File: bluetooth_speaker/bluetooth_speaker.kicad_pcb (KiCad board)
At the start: 2 copper layers, 40 parts, among them J1 Conn_Coaxial, J2 USB_C_Receptacle_USB2.0_16P, J3 282836-4, U1 MAX98357A, U2 XL4015, U3 CP2102N-A01-GQFN28, U4 ESP32-D0WD-V3, Y1 40MHz(±10 ppm)

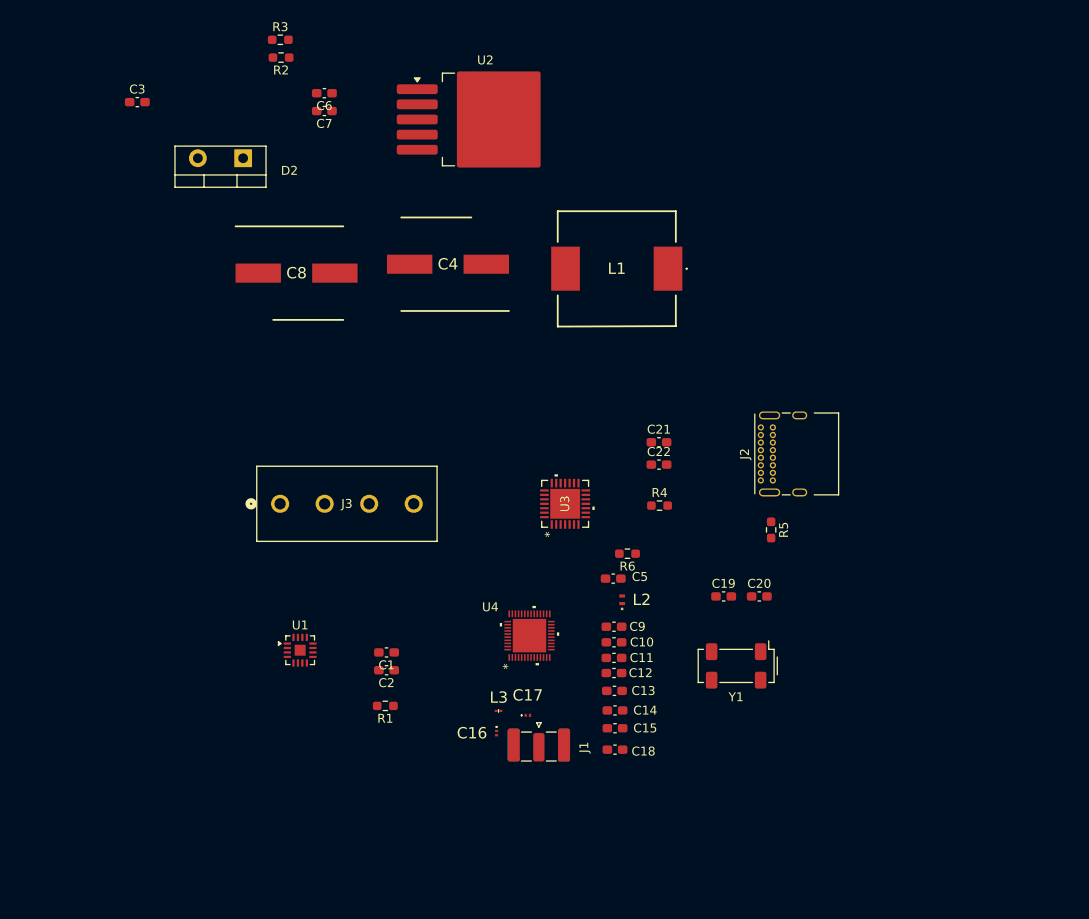
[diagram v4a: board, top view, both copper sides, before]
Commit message: Realigned components on PCB
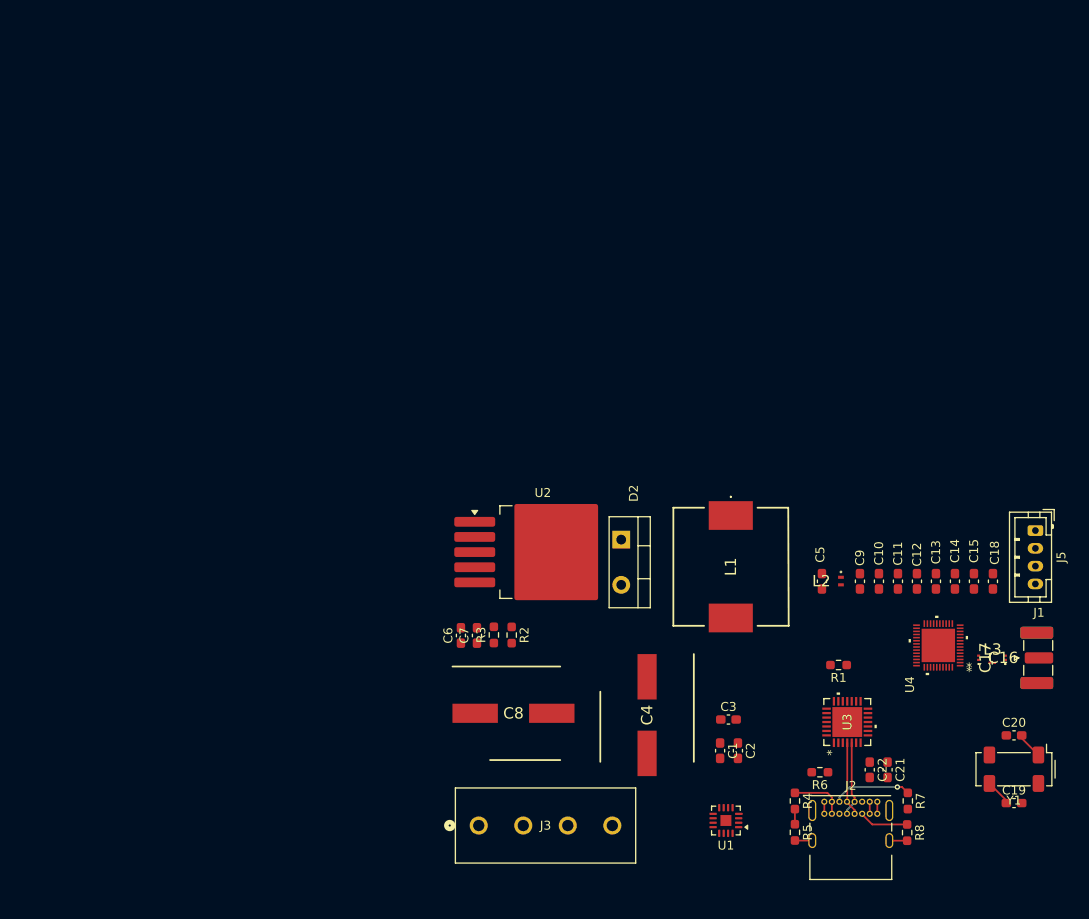
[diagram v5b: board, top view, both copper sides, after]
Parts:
- added J5: Conn_01x04_Pin, Connector_JST:JST_PH_B4B-PH-K_1x04_P2.00mm_Vertical, F.Cu at (181.0, 87.0)
- added R7: 5.1k, Resistor_SMD:R_0603_1608Metric_Pad0.98x0.95mm_HandSolder, F.Cu at (166.7, 117.4)
- added R8: 5.1k, Resistor_SMD:R_0603_1608Metric_Pad0.98x0.95mm_HandSolder, F.Cu at (166.6, 120.9)
- moved C3 96.0 mm to (146.5, 108.2)
- moved R3 71.0 mm to (120.2, 98.7), turned to 90 degrees
- moved R2 69.8 mm to (122.2, 98.7), turned to -90 degrees
- moved C6 62.8 mm to (116.5, 98.8), turned to 90 degrees
- moved C7 61.3 mm to (118.3, 98.8), turned to 90 degrees
- moved D2 60.3 mm to (134.5, 88.0), turned to -90 degrees
- moved J1 57.0 mm to (181.4, 101.3), turned to 0 degrees
- moved L3 55.7 mm to (176.2, 101.8)
- moved C4 55.3 mm to (137.4, 107.7), turned to -90 degrees
- moved C8 55.1 mm to (122.4, 107.5)
- moved C16 54.8 mm to (174.6, 101.3), turned to 90 degrees
- moved C17 54.0 mm to (177.6, 101.3), turned to 90 degrees
- moved U1 51.5 mm to (146.2, 119.6), turned to 180 degrees
- moved R1 51.1 mm to (158.9, 102.1)
- moved U2 49.0 mm to (125.7, 89.4)
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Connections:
- J2 pad A5: unconnected-(J2-CC1-PadA5) -> Net-(J2-CC1)
- J2 pad B5: unconnected-(J2-CC2-PadB5) -> Net-(J2-CC2)
- U4 pad 34: unconnected-(U4-GPIO5-Pad34) -> /BTN_VOL_DOWN
- U4 pad 35: unconnected-(U4-GPIO18-Pad35) -> /BTN_VOL_UP
- U4 pad 36: unconnected-(U4-GPIO23-Pad36) -> /BTN_PLAY
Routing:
- net Net-(J2-CC1): track 0.00 -> 8.92 mm, vias 0 -> 1
- net /USB-UART Converter/USB_D-: track 0.00 -> 8.46 mm
- net /USB-UART Converter/USB_D+: track 0.00 -> 8.34 mm
- net /USB-UART Converter/VBUS: track 0.00 -> 7.55 mm
- net GND: track 0.00 -> 6.66 mm
- net Net-(J2-CC2): track 0.00 -> 5.59 mm
- net /XTAL_N: track 0.00 -> 2.99 mm
- net /XTAL_P: track 0.00 -> 2.98 mm
- net Net-(U3-VBUS): track 0.00 -> 1.70 mm

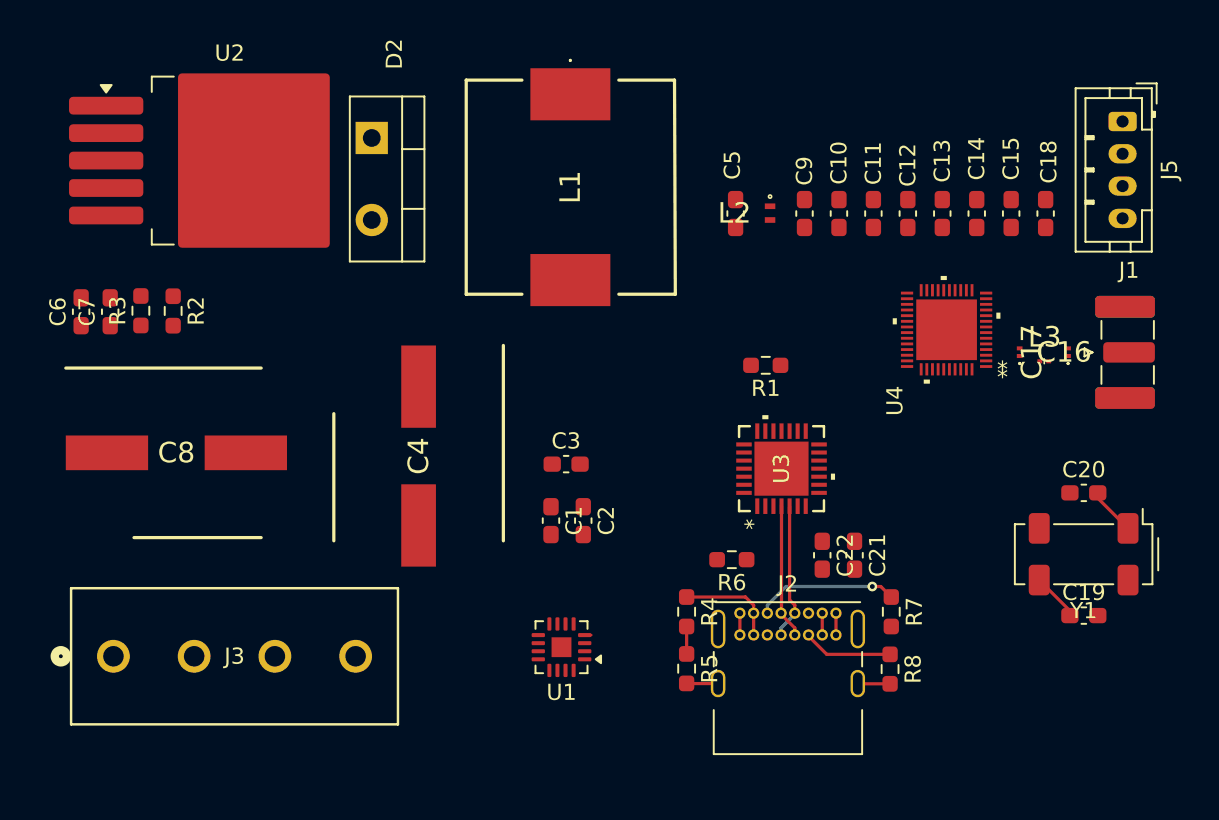
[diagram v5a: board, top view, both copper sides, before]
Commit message: Added auto-programming through CP2102
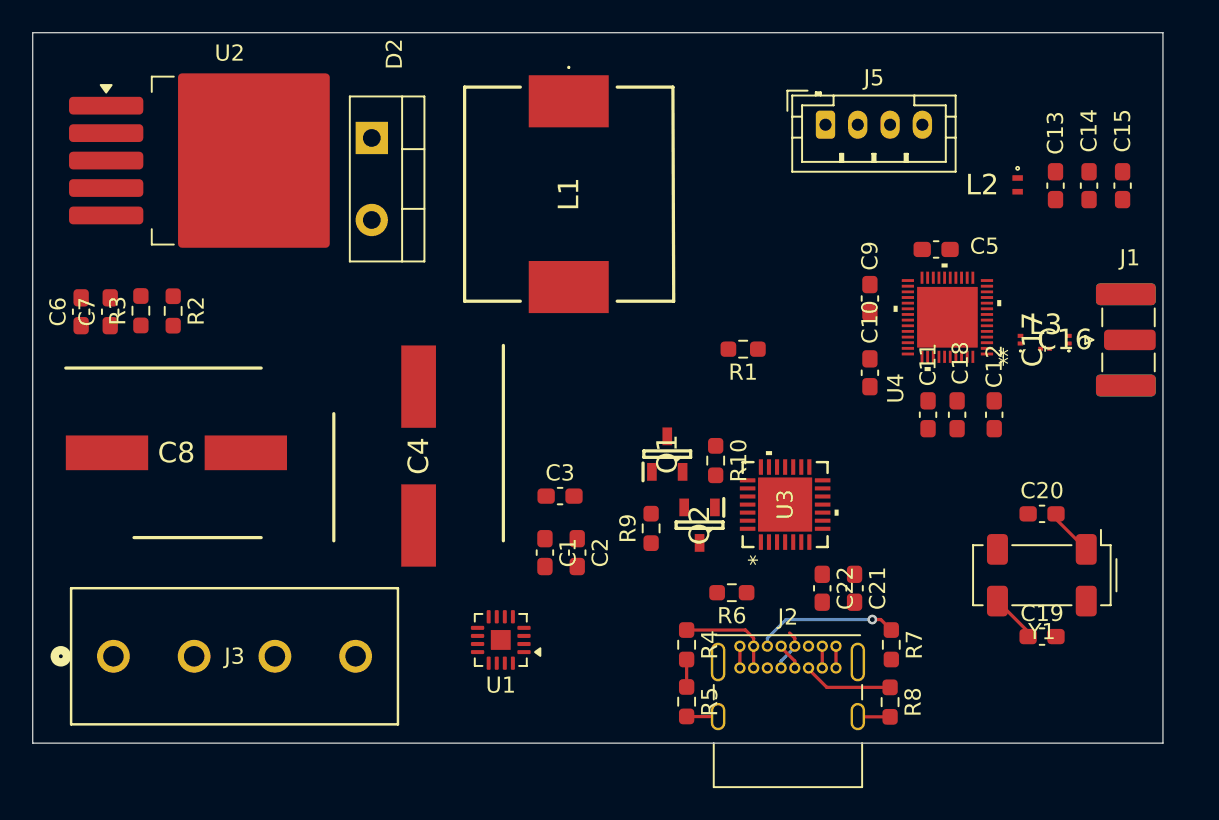
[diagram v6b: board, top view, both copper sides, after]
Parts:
- added Q1: SS8050-G, SamacSys_Parts:SOT95P240X115-3N, F.Cu at (152.8, 107.6)
- added Q2: SS8050-G, SamacSys_Parts:SOT95P240X115-3N, F.Cu at (154.8, 112.0)
- added R10: 10k, Resistor_SMD:R_0603_1608Metric_Pad0.98x0.95mm_HandSolder, F.Cu at (155.8, 108.0)
- added R9: 10k, Resistor_SMD:R_0603_1608Metric_Pad0.98x0.95mm_HandSolder, F.Cu at (151.8, 112.2)
- moved J5 18.4 mm to (162.6, 87.2), turned to 0 degrees
- moved L2 15.4 mm to (174.5, 90.9)
- moved C18 13.6 mm to (170.8, 105.2)
- moved C12 13.6 mm to (173.1, 105.2)
- moved C11 12.9 mm to (169.0, 105.2)
- moved C5 12.6 mm to (169.5, 94.9), turned to 180 degrees
- moved C10 10.0 mm to (165.4, 102.6)
- moved C13 7.22 mm to (176.8, 91.0)
- moved C14 7.17 mm to (178.9, 91.0)
- moved C15 7.11 mm to (181.0, 91.0)
- moved C9 6.64 mm to (165.4, 98.0)
- moved U1 3.79 mm to (142.5, 119.1)
- moved C19 2.90 mm to (176.0, 118.9)
- moved C20 2.90 mm to (176.0, 111.3)
- moved Y1 2.90 mm to (176.0, 115.1)
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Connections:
- U3 pad 24: unconnected-(U3-RTS-Pad24) -> Net-(Q1-E)
- U3 pad 28: unconnected-(U3-DTR-Pad28) -> Net-(Q2-C)
- U4 pad 23: unconnected-(U4-GPIO0-Pad23) -> /IO0
- U4 pad 9: unconnected-(U4-CHIP_PU-Pad9) -> /EN
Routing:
- net /USB-UART Converter/USB_D+: track 8.34 -> 1.74 mm
- net /USB-UART Converter/USB_D-: track 8.46 -> 2.66 mm
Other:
- board outline added: 70 x 44 mm

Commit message: again
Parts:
- moved L3 0.48 mm to (176.3, 100.6)
- moved C16 0.48 mm to (174.8, 100.0)
- moved C17 0.48 mm to (177.8, 100.0)
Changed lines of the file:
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@@
 	(footprint "SamacSys_Parts:LQP03TG3N1B02D"
 		(layer "F.Cu")
-		(at 176.2013 101.075)
+		(at 176.275 100.6)
 		(descr "0201 (0603) T=0.3±0.03mm")
 		(tags "Inductor")
@@
 	(footprint "SamacSys_Parts:GRM033D70J224ME01D"
 		(layer "F.Cu")
-		(at 174.6763 100.512 90)
+		(at 174.75 100.037 90)
 		(descr "GRM03")
 		(tags "Capacitor")
@@
 	(footprint "SamacSys_Parts:GRM033D70J224ME01D"
 		(layer "F.Cu")
-		(at 177.6763 100.512 90)
+		(at 177.75 100.037 90)
 		(descr "GRM03")
 		(tags "Capacitor")
@@
 	)
 	(segment
+		(start 181.525 100.525)
+		(end 181.6 100.6)
+		(width 0.15)
+		(layer "F.Cu")
+		(net 5)
+	)
+	(segment
+		(start 181.4513 100.525)
+		(end 181.525 100.525)
+		(width 0.15)
+		(layer "F.Cu")
+		(net 5)
+	)
+	(segment

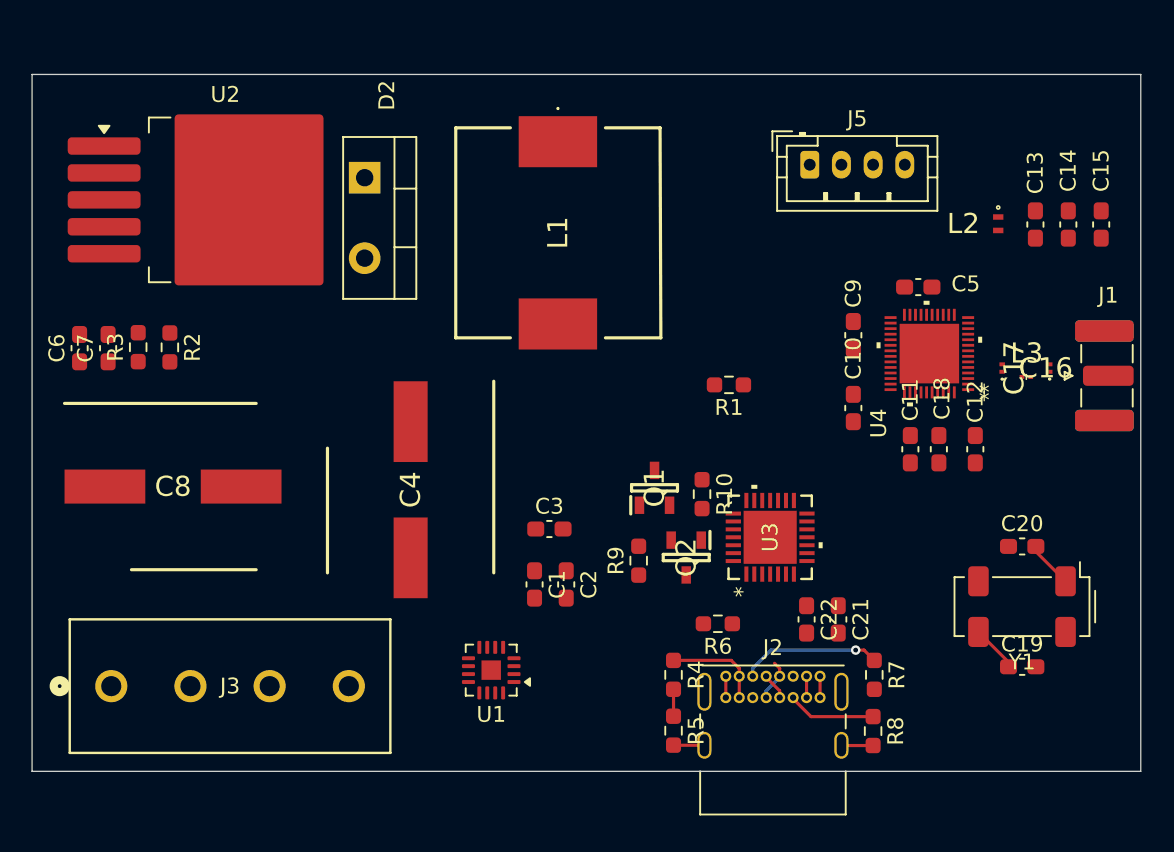
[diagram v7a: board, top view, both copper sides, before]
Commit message: Updated PCB traces
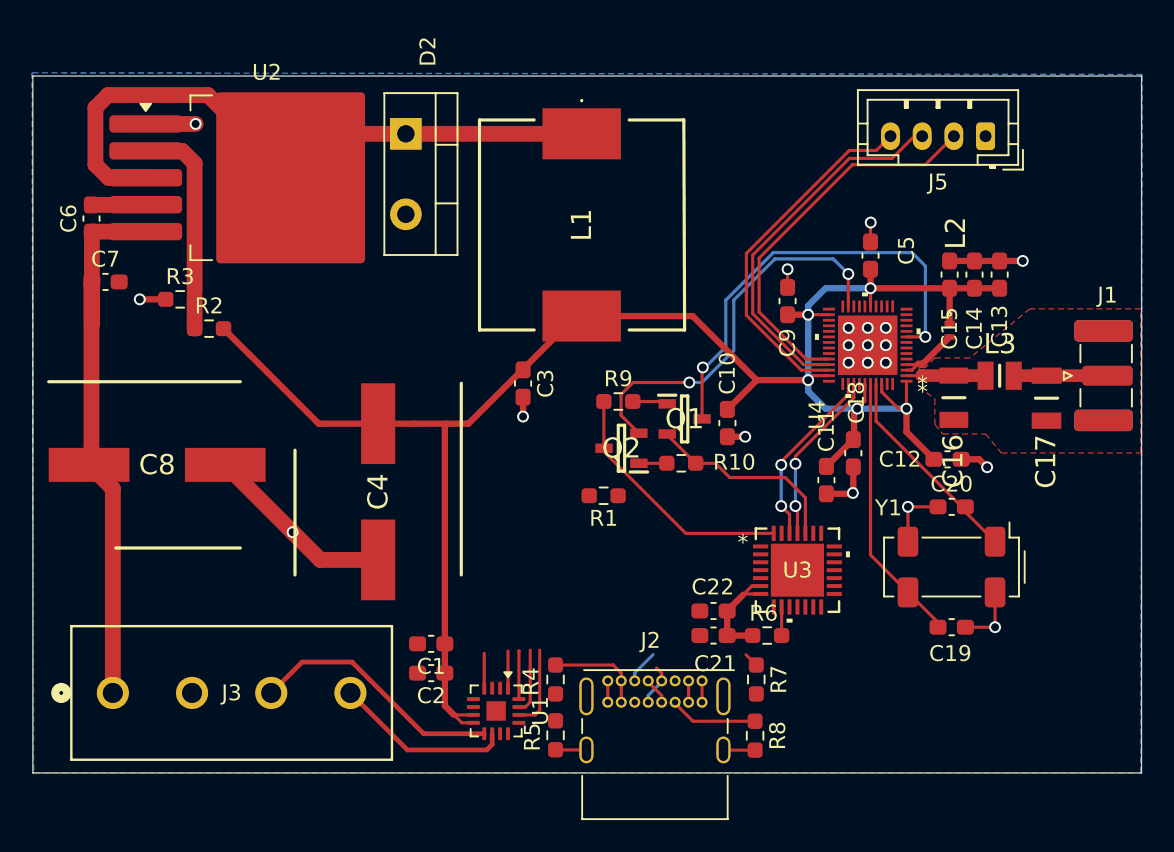
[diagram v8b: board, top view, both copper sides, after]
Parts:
- C16: footprint SamacSys_Parts:GRM033D70J224ME01D -> SamacSys_Parts:CAPC3216X94N
- C17: footprint SamacSys_Parts:GRM033D70J224ME01D -> SamacSys_Parts:CAPC3216X170N
- L3: footprint SamacSys_Parts:LQP03TG3N1B02D -> SamacSys_Parts:LQW2BAN11NG00L
- moved J5 11.2 mm to (173.7, 85.4), turned to 180 degrees
- moved R1 10.6 mm to (149.6, 108.1)
- moved C2 10.2 mm to (138.7, 119.3), turned to 180 degrees
- moved R9 10.1 mm to (150.5, 102.2), turned to 0 degrees
- moved C15 10.1 mm to (171.4, 94.1), turned to 90 degrees
- moved C3 9.34 mm to (144.5, 101.0), turned to -90 degrees
- moved C6 8.22 mm to (117.2, 90.6)
- moved Q2 8.02 mm to (150.7, 105.1), turned to 180 degrees
- moved C10 8.01 mm to (157.4, 103.5)
- moved C21 7.94 mm to (156.5, 116.9), turned to 180 degrees
- moved C1 7.53 mm to (138.7, 117.5), turned to 180 degrees
- moved J2 7.46 mm to (149.8, 119.8)
- moved R7 7.46 mm to (159.2, 119.7)
- moved R4 7.46 mm to (146.6, 119.7)
- moved R5 7.46 mm to (146.6, 123.2)
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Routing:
- net +3.3V: track 0.00 -> 124.4 mm, vias 0 -> 5
- net GND: track 6.66 -> 50.4 mm, vias 0 -> 21
- net Net-(D2-K): track 0.00 -> 41.5 mm
- net /Power/Batt+: track 0.00 -> 36.0 mm
- net /EN: track 0.00 -> 28.1 mm, vias 0 -> 2
- net /IO0: track 0.00 -> 25.1 mm, vias 0 -> 2
- net /BTN_VOL_DOWN: track 0.00 -> 24.5 mm
- net /BTN_VOL_UP: track 0.00 -> 23.7 mm
- net /BTN_PLAY: track 0.00 -> 22.7 mm
- net /Audio/AUDIO_OUT+: track 0.00 -> 16.1 mm
- net Net-(Q2-C): track 0.00 -> 16.0 mm
- net /XTAL_N: track 2.99 -> 17.1 mm
- net Net-(U2-FB): track 0.00 -> 13.4 mm
- net Net-(Q1-E): track 0.00 -> 13.3 mm
- net /U0RXD: track 0.00 -> 11.4 mm, vias 0 -> 2
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- added copper zone on B.Cu, net GND
- added copper zone on F.Cu, net GND
